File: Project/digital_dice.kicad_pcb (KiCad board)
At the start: 2 copper layers, 23 parts, among them J1 Conn_01x08, SW1 Conn_01x02, U1 74LS04, U2 74LS93, U3 74LS08, U4 74LS32, U5 LM7805_TO220

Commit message: routing complete
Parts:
- added C7: 1uF, Capacitor_THT:CP_Radial_D5.0mm_P2.50mm, F.Cu at (170.4, 153.9)
- added C8: 1uF, Capacitor_THT:CP_Radial_D5.0mm_P2.50mm, F.Cu at (152.2, 130.4)
- added D1: 1N4001, Diode_THT:D_DO-41_SOD81_P10.16mm_Horizontal, F.Cu at (129.1, 103.0)
- added H1: MountingHole_Pad, MountingHole:MountingHole_4.3mm_M4_Pad_Via, F.Cu at (122.0, 103.2)
- added H2: MountingHole_Pad, MountingHole:MountingHole_4.3mm_M4_Pad_Via, F.Cu at (186.0, 103.2)
- added H3: MountingHole_Pad, MountingHole:MountingHole_4.3mm_M4_Pad_Via, F.Cu at (122.0, 152.0)
- added H4: MountingHole_Pad, MountingHole:MountingHole_4.3mm_M4_Pad_Via, F.Cu at (186.0, 152.0)
- added J2: Conn_02x07_Odd_Even, Connector_PinHeader_2.54mm:PinHeader_2x07_P2.54mm_Vertical, F.Cu at (183.7, 116.3)
- J1: value Conn_01x08 -> Conn_01x04; footprint Connector_PinHeader_2.54mm:PinHeader_1x08_P2.54mm_Vertical -> Connector_PinHeader_2.54mm:PinHeader_1x04_P2.54mm_Vertical
- U1: value 74LS04 -> LM7805_TO220; footprint Package_DIP:DIP-14_W7.62mm -> Package_TO_SOT_THT:TO-220-3_Horizontal_TabDown
- U2: value 74LS93 -> 74LS04
- U5: value LM7805_TO220 -> 74LS93; footprint Package_TO_SOT_THT:TO-220-3_Vertical -> Package_DIP:DIP-14_W7.62mm
- moved U2 175.2 mm to (163.5, 147.5), turned to 90 degrees
- moved J1 167.3 mm to (186.2, 136.0)
- moved R1 160.0 mm to (157.2, 146.8), turned to -90 degrees
- moved R2 155.1 mm to (154.2, 146.8), turned to -90 degrees
- moved C3 153.5 mm to (158.7, 139.9), turned to 180 degrees
- moved C6 153.1 mm to (162.9, 151.9), turned to -90 degrees
- moved R3 149.2 mm to (170.3, 114.9)
- moved R4 148.7 mm to (170.3, 117.9)
- moved R5 148.3 mm to (170.3, 120.9)
- moved R6 147.9 mm to (170.3, 123.9)
- moved R7 147.4 mm to (170.3, 126.9)
- moved R8 147.0 mm to (170.3, 129.9)
- moved R9 146.6 mm to (170.3, 132.9)
- moved U3 146.6 mm to (134.2, 143.9), turned to 180 degrees
- moved U1 138.7 mm to (142.6, 103.0), turned to -90 degrees
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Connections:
- C1 pad 1: Net-(SW1-Pin_1) -> VBAT
- C1 pad 2: Net-(C1-Pad2) -> GND
- C2 pad 1: Net-(C2-Pad1) -> VCC
- C2 pad 2: Net-(C2-Pad2) -> GND
- C6 pad 1: VCC -> Net-(SW1-Pin_1)
- C6 pad 2: GND -> Net-(C6-Pad2)
- J1 pad 1: LED1 -> ~{Q0}
- J1 pad 2: LED2 -> ~{Q1}
- J1 pad 3: LED3 -> ~{Q2}
- J1 pad 4: LED4 -> GND
- R1 pad 2: Net-(C1-Pad2) -> Net-(C6-Pad2)
- R2 pad 2: Net-(C2-Pad1) -> Net-(C7-Pad1)
- U1 pad 1: Net-(C2-Pad1) -> VBAT
- U1 pad 2: Net-(SW1-Pin_1) -> GND
- U1 pad 3: Net-(C1-Pad2) -> VCC
- U2 pad 1: Q0 -> Net-(C7-Pad1)
- U2 pad 10: GND -> ~{Q1}
- U2 pad 11: unconnected-(U2-Q3-Pad11) -> Q1
- U2 pad 12: Q0 -> g
- U2 pad 13: (no net) -> Q0
- U2 pad 14: Unstable_Clock -> VCC
- U2 pad 2: Q1 -> Net-(SW1-Pin_1)
- U2 pad 3: Q2 -> Net-(C6-Pad2)
- U2 pad 4: (no net) -> Net-(C7-Pad2)
- U2 pad 5: VCC -> Q2
- U2 pad 6: (no net) -> ~{Q2}
- U2 pad 7: (no net) -> GND
- U2 pad 8: Q2 -> ~{Q0}
- U2 pad 9: Q1 -> Q0
- U3 pad 1: Q0 -> GND
- U3 pad 10: GND -> Q0
- U3 pad 2: Q2 -> GND
- U3 pad 3: b -> unconnected-(U3-Pad3)
- U3 pad 8: unconnected-(U3-Pad8) -> b
- U3 pad 9: GND -> Q2
- U5 pad 1: Net-(BATT1-Pin_1) -> Q0
- U5 pad 2: GND -> Q1
- U5 pad 3: VCC -> Q2
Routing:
- net VCC: track 0.00 -> 114.8 mm, vias 0 -> 2
- net Q2: track 0.00 -> 93.3 mm
- net Q0: track 0.00 -> 83.2 mm
- net Q1: track 0.00 -> 63.1 mm
- net b: track 0.00 -> 60.9 mm
- net a: track 0.00 -> 33.3 mm
- net Net-(U3-Pad6): track 0.00 -> 29.1 mm
- net Net-(C7-Pad1): track 0.00 -> 28.8 mm
- net Net-(SW1-Pin_1): track 0.00 -> 21.6 mm
- net ~{Q1}: track 0.00 -> 15.2 mm
- net Net-(C6-Pad2): track 0.00 -> 15.0 mm
- net Unstable_Clock: track 0.00 -> 13.6 mm
- net VBAT: track 0.00 -> 13.5 mm
- net c: track 0.00 -> 13.1 mm
- net ~{Q2}: track 0.00 -> 12.6 mm
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- added copper zone on B.Cu, net GND
- added copper zone on F.Cu, net GND
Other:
- board outline added: 76 x 60.8 mm
- board text added: "GND"
- board text added: "a"
- board text added: "b"
- board text added: "c"
- board text added: "d"
- board text added: "e"
- board text added: "f"
- board text added: "g"
- board text added: "~{Q0}"
- board text added: "~{Q1}"
- board text added: "~{Q2}"

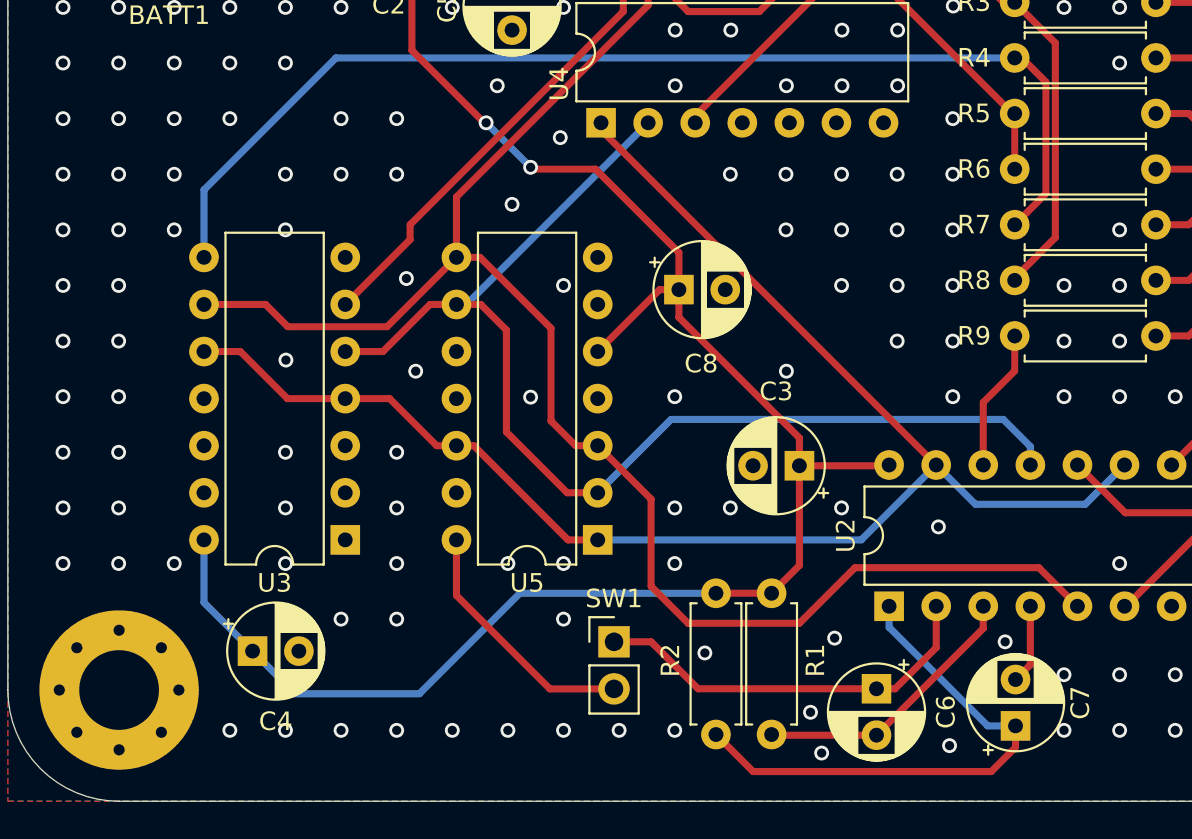
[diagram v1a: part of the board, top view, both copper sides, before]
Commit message: fix #3
Latch was not unstable. Changed R1 and R2 to pulldown
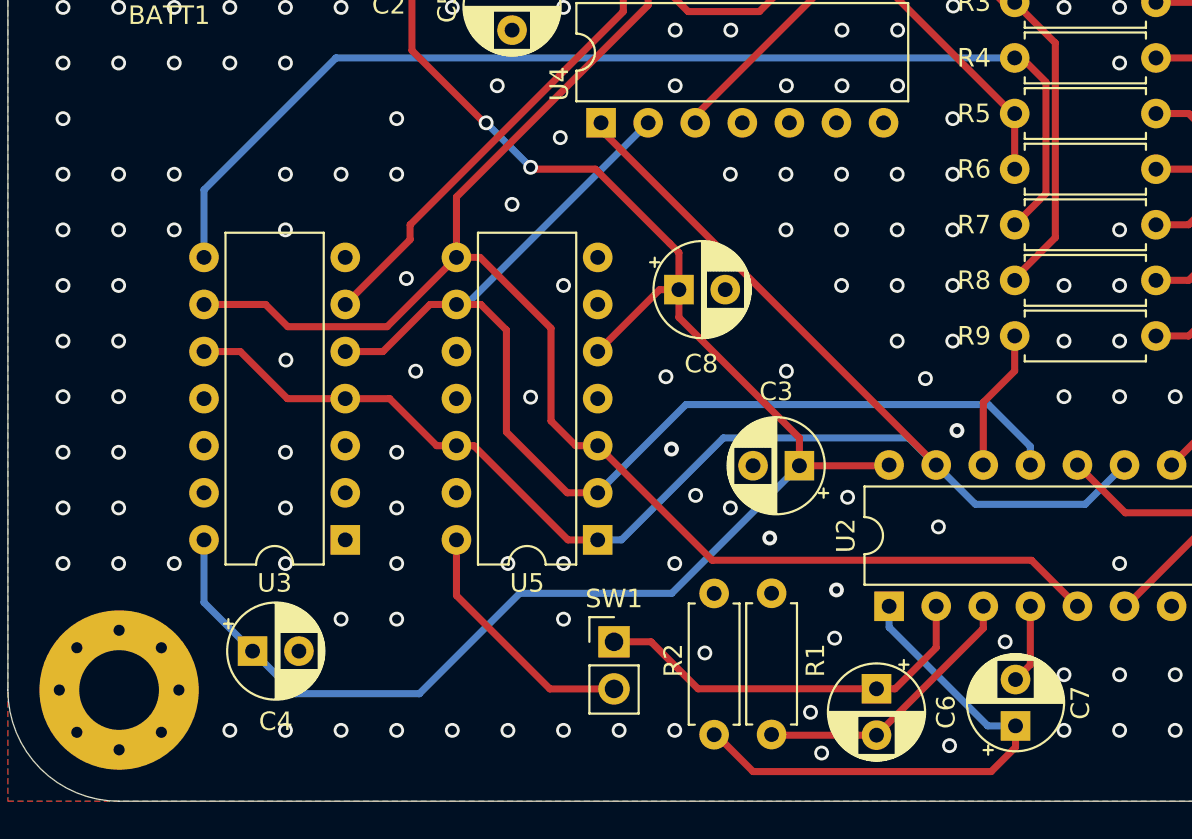
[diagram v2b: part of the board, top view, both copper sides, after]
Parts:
- moved R2 7.63 mm to (154.1, 154.4), turned to 90 degrees
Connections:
- R1 pad 1: VCC -> GND
- R2 pad 1: VCC -> Net-(C7-Pad1)
- R2 pad 2: Net-(C7-Pad1) -> GND
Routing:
- net Q2: track 93.3 -> 88.0 mm
- net VCC: track 114.8 -> 111.6 mm
- net Q0: track 83.2 -> 84.5 mm
- net Q1: track 63.1 -> 63.7 mm
